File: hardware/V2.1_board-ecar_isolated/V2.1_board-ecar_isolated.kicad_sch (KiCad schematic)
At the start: 99 parts, among them IC1 ATMEGA8A-P, J1 2x BATT IN, J10 24V, J11 18V, J12 5V, J13 Analog-in-2 0-5V, J14 IGBT [GND, Gate], J15 Analog-in-3 - 30to5 (batt), J17 2x Switch (to 5V), J18 Relay contacts [NO, COM, NC], J19 2x 5V, J2 ST 2x GND, J20 ADC Battery, J21 ADC reserve, J22 ADC Gas-pedal, J23 2x 24V filtered, J24 Fan [GND-supp, Diode, Mosfet], J3 2x 24V filtered, J4 ST 2x GND, J5 PWM-Signal, J6 LED 3,2V 20mA [-, +], J7 Gas Pedal, J8 Gate, J9 BATT, K1 LEG-5, P1 ISP, Q1 BC547, Q2 IRFZ24N, Q3 BC547, U1 LM7818CT, U2 LM2576T-5, U3 TC429

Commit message: pcb: Schematic: Isolated supply, Optocouplers...
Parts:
- removed C1: 100u, Capacitor_THT:CP_Radial_D8.0mm_P5.00mm, symbol Device:C_Polarized
- removed C16: 100n, Capacitor_THT:C_Disc_D7.0mm_W2.5mm_P5.00mm, symbol Device:C
- removed C5: 1000u, Capacitor_THT:CP_Radial_D10.0mm_P5.00mm, symbol Device:C_Polarized
- removed D2: 1N5822, Diode_THT:D_DO-201AD_P15.24mm_Horizontal, symbol Diode:1N5822
- removed D7: 5V1, Diode_THT:D_A-405_P10.16mm_Horizontal, symbol Device:D_Zener
- removed J13: Analog-in-2 0-5V, TerminalBlock:TerminalBlock_bornier-2_P5.08mm, symbol Connector:Screw_Terminal_01x02
- removed J15: Analog-in-3 - 30to5 (batt), TerminalBlock:TerminalBlock_bornier-2_P5.08mm, symbol Connector:Screw_Terminal_01x02
- removed J20: ADC Battery, Connector_PinHeader_1.00mm:PinHeader_1x01_P1.00mm_Vertical, symbol Connector:Conn_01x01_Pin
- removed L1: 100u, Inductor_THT:L_Radial_D8.7mm_P5.00mm_Fastron_07HCP, symbol Device:L
- removed Q3: BC547, Package_TO_SOT_THT:TO-92L, symbol Transistor_BJT_AKL:BC547
- removed R17: 22k, Resistor_THT:R_Axial_DIN0207_L6.3mm_D2.5mm_P10.16mm_Horizontal, symbol control-rescue:R
- removed R20: 2k2, Resistor_THT:R_Axial_DIN0207_L6.3mm_D2.5mm_P10.16mm_Horizontal, symbol control-rescue:R
- removed R21: 470, Resistor_THT:R_Axial_DIN0207_L6.3mm_D2.5mm_P10.16mm_Horizontal, symbol Device:R
- removed U2: LM2576T-5, Package_TO_SOT_THT:TO-220-5_Vertical, symbol Regulator_Switching:LM2576T-5
- added C1: 100n, Capacitor_THT:C_Disc_D7.0mm_W2.5mm_P5.00mm, symbol Device:C
- added J13: ADC reserve, TerminalBlock:TerminalBlock_bornier-3_P5.08mm, symbol Connector:Screw_Terminal_01x03
- added J16: UART [TX, RX, GND], Connector_PinHeader_2.54mm:PinHeader_1x03_P2.54mm_Vertical, symbol Connector:Conn_01x03_Pin
- added OC2, OC3, OC4: LTV-817, Package_DIP:DIP-4_W10.16mm_LongPads, symbol Optocoupler_AKL:LTV-817
- added PS1: RSO-2405S, RSO-2405S:CONV_RSO-2405S, symbol RSO-2405S:RSO-2405S
- added R15: 330, Resistor_THT:R_Axial_DIN0207_L6.3mm_D2.5mm_P10.16mm_Horizontal, symbol treiber-rescue:R
- added R21, R28: 200, Resistor_THT:R_Axial_DIN0207_L6.3mm_D2.5mm_P10.16mm_Horizontal, symbol treiber-rescue:R
- added R30: 150k, Resistor_THT:R_Axial_DIN0207_L6.3mm_D2.5mm_P10.16mm_Horizontal, symbol control-rescue:R
- added R31: 100k, Resistor_THT:R_Axial_DIN0207_L6.3mm_D2.5mm_P10.16mm_Horizontal, symbol control-rescue:R
- added R32: 1k, Resistor_THT:R_Axial_DIN0207_L6.3mm_D2.5mm_P10.16mm_Horizontal, symbol control-rescue:R
- added RV1: 500k, Potentiometer_THT:Potentiometer_Piher_PT-10-V10_Vertical, symbol Device:R_Potentiometer_Trim
- added TP1, TP2: TestPoint, symbol Connector:TestPoint
- added U4: LM358N, Package_DIP_AKL:DIP-8_W7.62mm_LongPads, symbol Amplifier_Operational_AKL:LM358N
- J2: value ST 2x GND -> ST 2x GND power
- J4: value ST 2x GND -> ST 2x GND 5V
- K1: value LEG-5 -> 24V relay
- R16: value 100k -> 10k
- R18: value 1k -> 10k
- R19: value 22k -> 10k
- R6: value 320 -> 200
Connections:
- net analog2 (30V Batt) is gone; now on net battery-threshold: IC1.23 ((ADC0)PC0)
- net +18V: now also RV1.1, U4.8 (V+)
- net +24V filtered: now also D11.1 (K), K1.5, R18.2, PS1.2 (+VIN), R30.1
- net +5V: now also R16.1, J13.3 (Pin_3), PS1.6 (+VOUT); no longer D11.1 (K), K1.5
- net GND: now also P1.4, C1.2, J13.1 (Pin_1), J16.3 (Pin_3), OC2.2, OC3.2, OC4.3, PS1.7 (-VOUT), R15.2, TP1.1; no longer C10.2, C12.2, C13.2, C14.2, C19.2, C2.2, C3.2, C4.2, C9.2, D1.2 (A), D3.1 (A1), J14.1 (Pin_1), J2.1 (Pin_1), J2.2 (Pin_2), J24.3 (Pin_3), OC1.3, Q2.3 (S), R10.2, R19.1, U1.2 (GND), U3.4 (GND), U3.5 (GND)
- net Mosfet (fan): now also R28.2; no longer R18.2
- net Relay (light): now also R21.2
- net battery-threshold: now reaches R16.2
- net battery-threshold: now also OC4.4
- net at C11.1, D5.1 (K), J22.1 (Pin_1)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: now also C1.1
- net at R14.1: now also J13.2 (Pin_2)
- net at Q2.1 (G), R18.1, R19.2: now also OC2.4
- net UART_RX: now reaches IC1.2 ((RXD)PD0)
- net UART_RX: now also J16.2 (Pin_2)
- net UART_TX: now reaches IC1.3 ((TXD)PD1)
- net UART_TX: now also J16.1 (Pin_1)
- net at IC1.9 (PB6(XTAL1/TOSC1)): now also R15.1
- net at D11.2 (A), K1.2: now also OC3.4
- new net: R30.2, R31.1, U4.2 (-)
- new net: OC4.1, R32.2
- new net: RV1.2, U4.3 (+)
- new net: OC2.1, R28.1
- new net: R32.1, U4.1
- new net: OC3.1, R21.1
- new net GNDPWR: C10.2, C12.2, C13.2, C14.2, C19.2, C2.2, C3.2, C4.2, C9.2, D1.2 (A), D3.1 (A1), J14.1 (Pin_1), J2.1 (Pin_1), J2.2 (Pin_2), J24.3 (Pin_3), OC1.3, OC2.3, OC3.3, OC4.2, PS1.1 (-VIN), Q2.3 (S), R10.2, R19.1, R31.2, RV1.3, TP2.1, U1.2 (GND), U3.4 (GND), U3.5 (GND), U4.4 (V-)
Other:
- note added: "5V Supply (isolated dc-dc converter)"
- note added: "Batt-voltage threshold signal"
- note added: "CTRL: high = OFF/low-power open = ON"
- note added: "Input voltage range: 9V to 36V"
- note added: "TODO: Test if optocoupler can handle relay directly"
- note added: "UART connector"
- note added: "note: configure all unused pins as output and set to high at startup to prevent potential noise issues"
- note removed: "3A overcurrent safe"
- note removed: "5V Supply (buck converter)"
- note removed: "7-40V"
- note removed: "ADC Battery voltage"
- moved on the sheet: C11, C12, C13, C14, C15, D5, D6, D9, F4, J14, J19, J2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

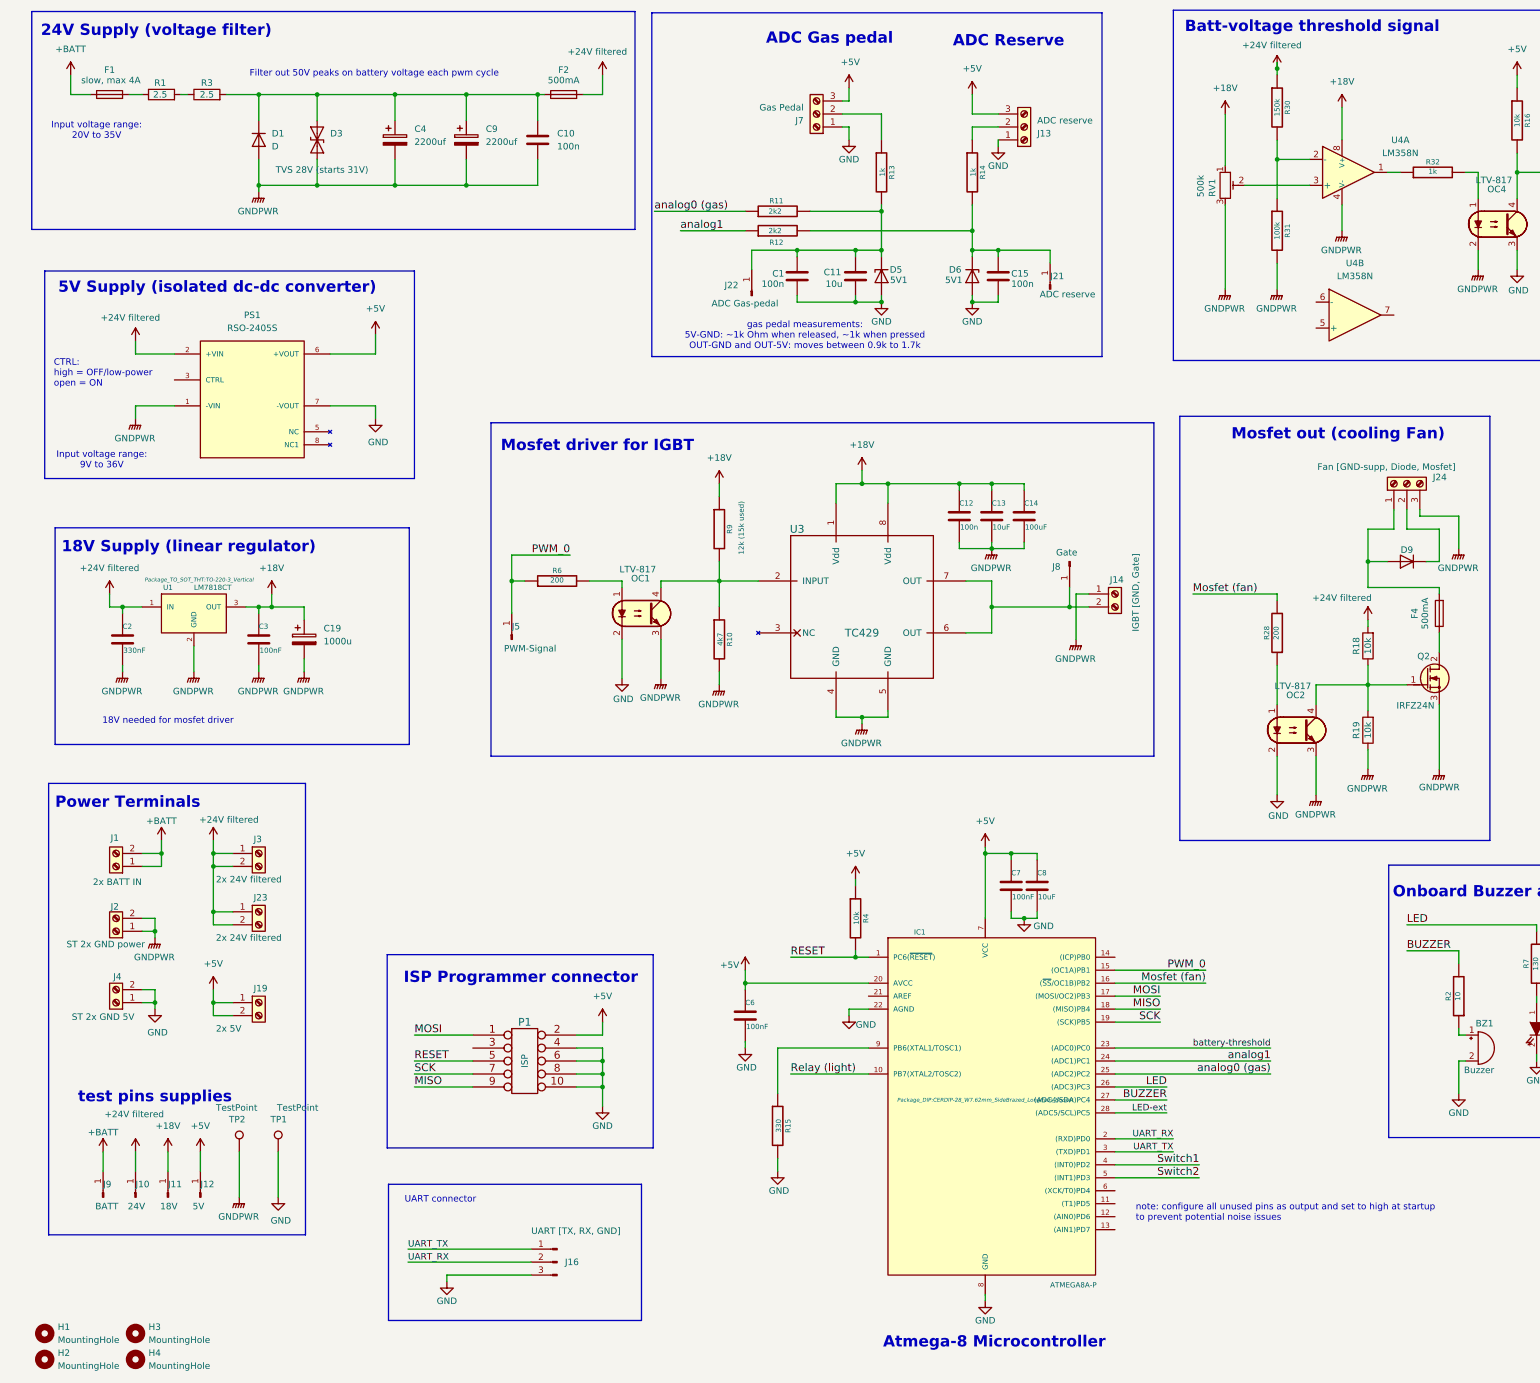
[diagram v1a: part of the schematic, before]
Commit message: pcb: small additions, begin footprint placment
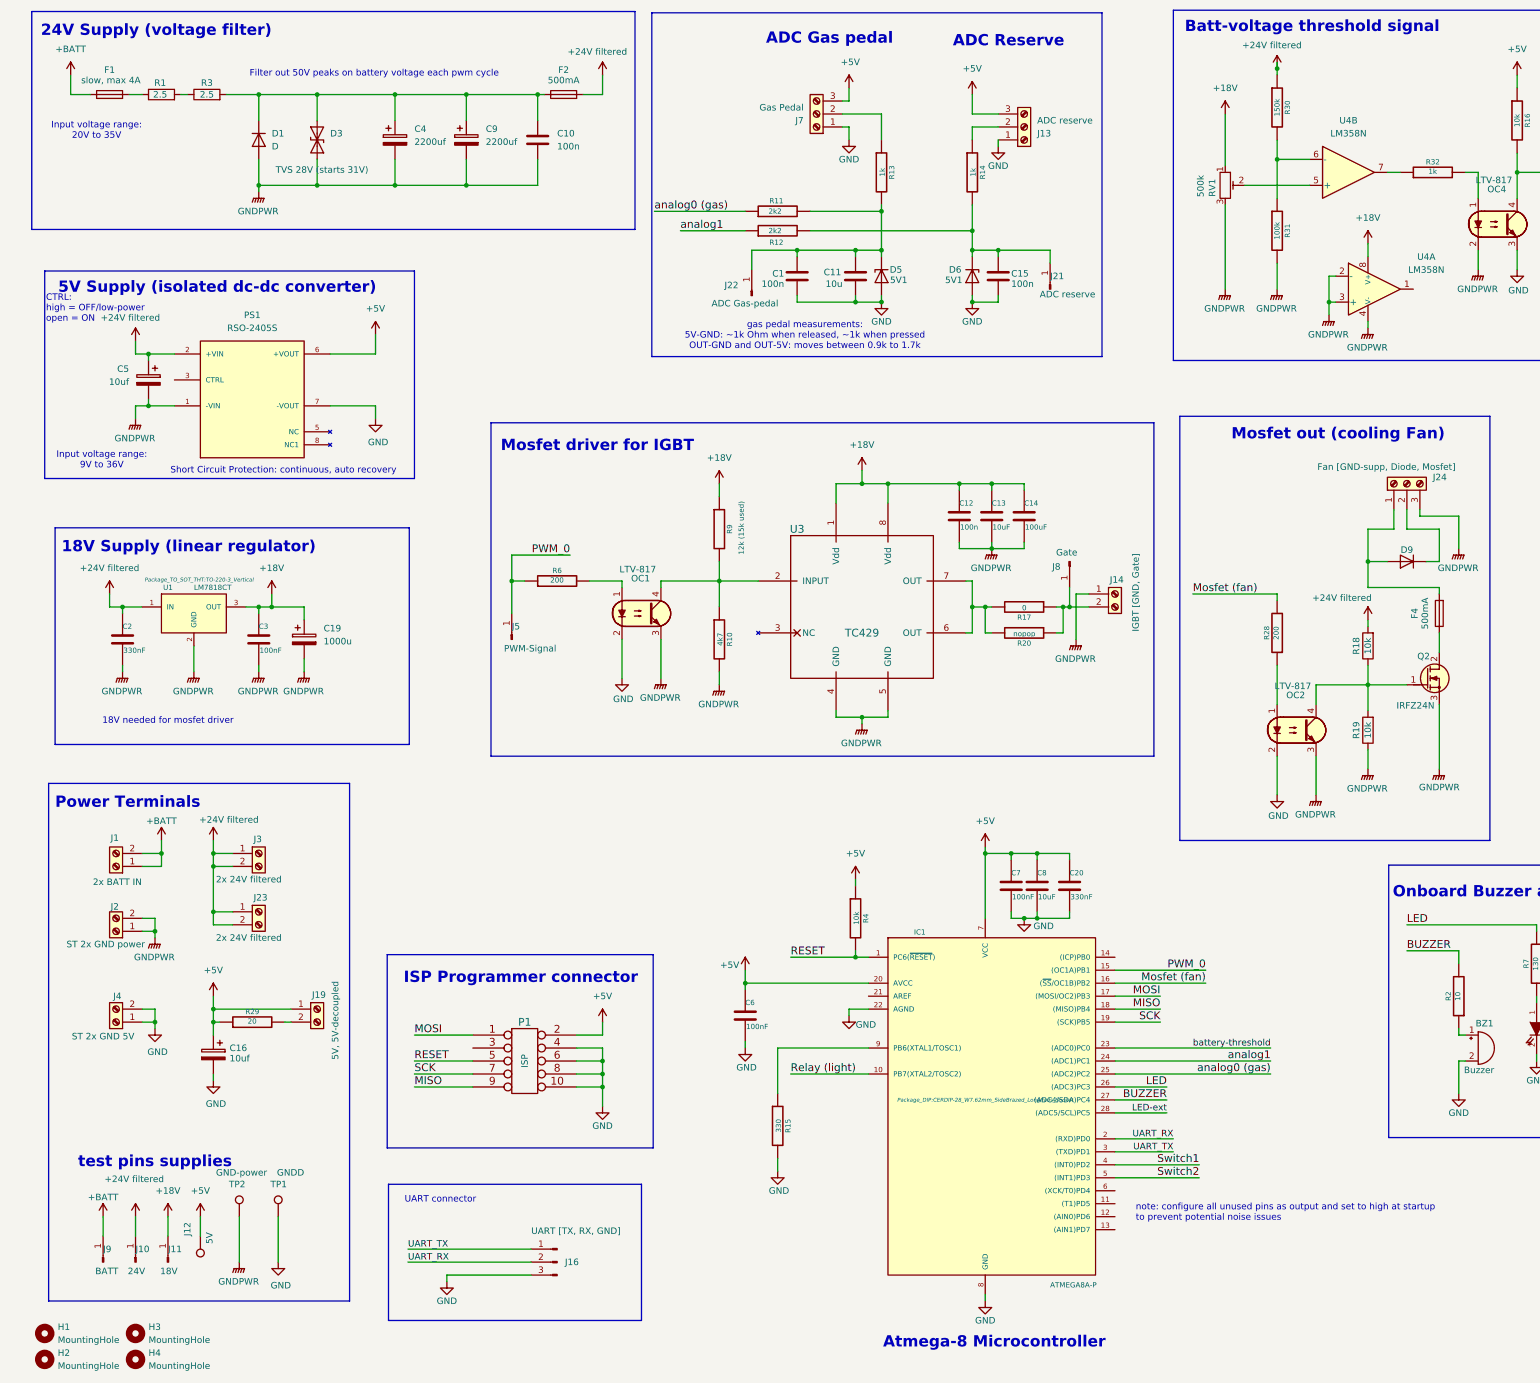
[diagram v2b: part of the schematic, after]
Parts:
- added C16, C5: 10uf, Capacitor_THT:CP_Radial_D5.0mm_P2.50mm, symbol Device:C_Polarized
- added C20: 330nF, Capacitor_THT:C_Disc_D8.0mm_W5.0mm_P5.00mm, symbol treiber-rescue:C
- added R17: 0, Resistor_THT:R_Axial_DIN0207_L6.3mm_D2.5mm_P10.16mm_Horizontal, symbol treiber-rescue:R
- added R20: nopop, Resistor_THT:R_Axial_DIN0207_L6.3mm_D2.5mm_P10.16mm_Horizontal, symbol treiber-rescue:R
- added R29: 20, Resistor_THT:R_Axial_DIN0207_L6.3mm_D2.5mm_P10.16mm_Horizontal, symbol treiber-rescue:R
- J12: symbol Connector:Conn_01x01_Pin -> Connector:TestPoint
- J19: value 2x 5V -> 5V, 5V-decoupled
- TP1: value TestPoint -> GNDD; footprint (none) -> Connector_PinHeader_1.00mm:PinHeader_1x01_P1.00mm_Vertical
- TP2: value TestPoint -> GND-power; footprint (none) -> Connector_PinHeader_1.00mm:PinHeader_1x01_P1.00mm_Vertical
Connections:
- net +24V filtered: now also C5.1
- net +5V: now also C16.1, C20.1, R29.1; no longer J19.2 (Pin_2)
- net GND: now also C16.2, C20.2
- net GNDPWR: now also U4.2 (-), U4.3 (+), C5.2
- net at J14.2 (Pin_2), J8.1 (Pin_1): now also R17.1, R20.1; no longer U3.6 (OUT), U3.7 (OUT)
- net at R30.2, R31.1: now also U4.6 (-); no longer U4.2 (-)
- net at U4.5 (+): now also RV1.2
- net at U4.7: now also R32.1
- net at U4.1: no longer R32.1
- new net: J19.2 (Pin_2), R29.2
- new net: R17.2, R20.2, U3.6 (OUT), U3.7 (OUT)
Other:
- note added: "Short Circuit Protection: continuous, auto recovery"
- moved on the sheet: J10, J11, J19, J4, J9, TP1, TP2, U4A, U4B
